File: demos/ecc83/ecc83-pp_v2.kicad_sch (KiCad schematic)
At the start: 15 parts, among them P1 IN, P2 OUT, P3 POWER, P4 CONN_2, P5 CONN_1, P6 CONN_1, P7 CONN_1, P8 CONN_1, U1 ECC83

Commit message: Demos update
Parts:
- U: renamed from R1; value 1.5K -> (none); footprint Resistor_THT:R_Axial_DIN0207_L6.3mm_D2.5mm_P7.62mm_Horizontal -> (none)
- U: renamed from R2; value 1.5K -> (none); footprint Resistor_THT:R_Axial_DIN0207_L6.3mm_D2.5mm_P7.62mm_Horizontal -> (none)
- U: renamed from R4; value 47K -> (none); footprint Resistor_THT:R_Axial_DIN0207_L6.3mm_D2.5mm_P7.62mm_Horizontal -> (none)
- U: renamed from R3; value 100K -> (none); footprint Resistor_THT:R_Axial_DIN0207_L6.3mm_D2.5mm_P7.62mm_Horizontal -> (none)
- U: renamed from C2; value 680nF -> (none); footprint Capacitors_THT:C_Axial_L12.0mm_D6.5mm_P20.00mm_Horizontal -> (none)
- U: renamed from P1; value IN -> (none); footprint Connector_PinHeader_2.54mm:PinHeader_1x02_P2.54mm_Vertical -> (none)
- U: renamed from P2; value OUT -> (none); footprint Connector_PinHeader_2.54mm:PinHeader_1x02_P2.54mm_Vertical -> (none)
- U: renamed from P3; value POWER -> (none); footprint Connector_PinHeader_2.54mm:PinHeader_1x02_P2.54mm_Vertical -> (none)
- U: renamed from C1; value 10uF -> (none); footprint Capacitor_THT:CP_Radial_D12.5mm_P7.50mm -> (none)
- U: renamed from P4; value CONN_2 -> (none); footprint Connector_PinHeader_2.54mm:PinHeader_1x02_P2.54mm_Vertical -> (none)
- U: renamed from U1; value ECC83 -> (none); footprint Valve:Valve_ECC-83-2 -> (none)
- U: renamed from P5; value CONN_1 -> (none); footprint connect:1pin -> (none)
- U: renamed from P6; value CONN_1 -> (none); footprint connect:1pin -> (none)
- U: renamed from P7; value CONN_1 -> (none); footprint connect:1pin -> (none)
- U: renamed from P8; value CONN_1 -> (none); footprint connect:1pin -> (none)
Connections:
- net at U.1, U.7 (G): now also U.6 (A); no longer U.1 (A)
- net at U.1: now also U.8 (K); no longer U.3 (K)
- net at U.1, U.2 (PM): now also U.7 (G); no longer U.2 (G)
- net at U.2 (PM): no longer U.9 (F2)
- now unconnected: U.1 (P1)

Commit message: Demos update.
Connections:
- net at U.1, U.7 (G): now also U.1 (A); no longer U.6 (A)
- net at U.1: now also U.3 (K); no longer U.8 (K)
- net at U.1, U.2 (PM): now also U.2 (G); no longer U.7 (G)
- net at U.1 (P1): now also U.4 (F1), U.5 (F1)
- net at U.2 (PM): now also U.9 (F2)
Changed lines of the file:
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@@
-(kicad_sch (version 20220404) (generator eeschema)
+(kicad_sch (version 20220822) (generator eeschema)
   (paper "A4")
   (title_block
@@
     (pin "7")
     (pin "8")
+  )
+  (symbol (lib_id "ecc83_schlib:ECC83") (at 165.1 106.68 0) (unit 2)
+    (in_bom yes) (on_board yes)
+    (default_instance (reference "U") (unit 1) (value "") (footprint ""))
+    (property "Reference" "U" (id 0) (at 177.8 104.14 0)
+      (effects (font (size 1.27 1.27)))
+    )
+    (property "Value" "" (id 1) (at 177.8 106.68 0)
+      (effects (font (size 1.27 1.27)))
+    )
+    (property "Footprint" "" (id 2) (at 177.8 109.22 0)
+      (effects (font (size 0.762 0.762)))
+    )
+    (property "Datasheet" "" (id 3) (at 165.1 106.68 0)
+      (effects (font (size 1.524 1.524)) hide)
+    )
     (pin "1")
     (pin "2")
     (pin "3")
+  )
+  (symbol (lib_id "ecc83_schlib:ECC83") (at 99.06 77.47 0) (unit 3)
+    (in_bom yes) (on_board yes)
+    (default_instance (reference "U") (unit 1) (value "") (footprint ""))
+    (property "Reference" "U" (id 0) (at 106.68 74.93 0)
+      (effects (font (size 1.27 1.27)))
+    )
+    (property "Value" "" (id 1) (at 107.95 77.47 0)
+      (effects (font (size 1.27 1.27)))
+    )
+    (property "Footprint" "" (id 2) (at 111.76 80.01 0)
+      (effects (font (size 0.762 0.762)))
+    )
+    (property "Datasheet" "" (id 3) (at 99.06 77.47 0)
+      (effects (font (size 1.524 1.524)) hide)
+    )
     (pin "4")
     (pin "5")
-    (pin "9")
-  )
-  (symbol (lib_id "ecc83_schlib:ECC83") (at 165.1 106.68 0) (unit 1)
-    (in_bom yes) (on_board yes)
-    (default_instance (reference "U") (unit 1) (value "") (footprint ""))
-    (property "Reference" "U" (id 0) (at 177.8 104.14 0)
-      (effects (font (size 1.27 1.27)))
-    )
-    (property "Value" "" (id 1) (at 177.8 106.68 0)
-      (effects (font (size 1.27 1.27)))
-    )
-    (property "Footprint" "" (id 2) (at 177.8 109.22 0)
-      (effects (font (size 0.762 0.762)))
-    )
-    (property "Datasheet" "" (id 3) (at 165.1 106.68 0)
-      (effects (font (size 1.524 1.524)) hide)
-    )
-    (pin "6")
-    (pin "7")
-    (pin "8")
-    (pin "1")
-    (pin "2")
-    (pin "3")
-    (pin "4")
-    (pin "5")
-    (pin "9")
-  )
-  (symbol (lib_id "ecc83_schlib:ECC83") (at 99.06 77.47 0) (unit 1)
-    (in_bom yes) (on_board yes)
-    (default_instance (reference "U") (unit 1) (value "") (footprint ""))
-    (property "Reference" "U" (id 0) (at 106.68 74.93 0)
-      (effects (font (size 1.27 1.27)))
-    )
-    (property "Value" "" (id 1) (at 107.95 77.47 0)
-      (effects (font (size 1.27 1.27)))
-    )
-    (property "Footprint" "" (id 2) (at 111.76 80.01 0)
-      (effects (font (size 0.762 0.762)))
-    )
-    (property "Datasheet" "" (id 3) (at 99.06 77.47 0)
-      (effects (font (size 1.524 1.524)) hide)
-    )
-    (pin "6")
-    (pin "7")
-    (pin "8")
-    (pin "1")
-    (pin "2")
-    (pin "3")
-    (pin "4")
-    (pin "5")

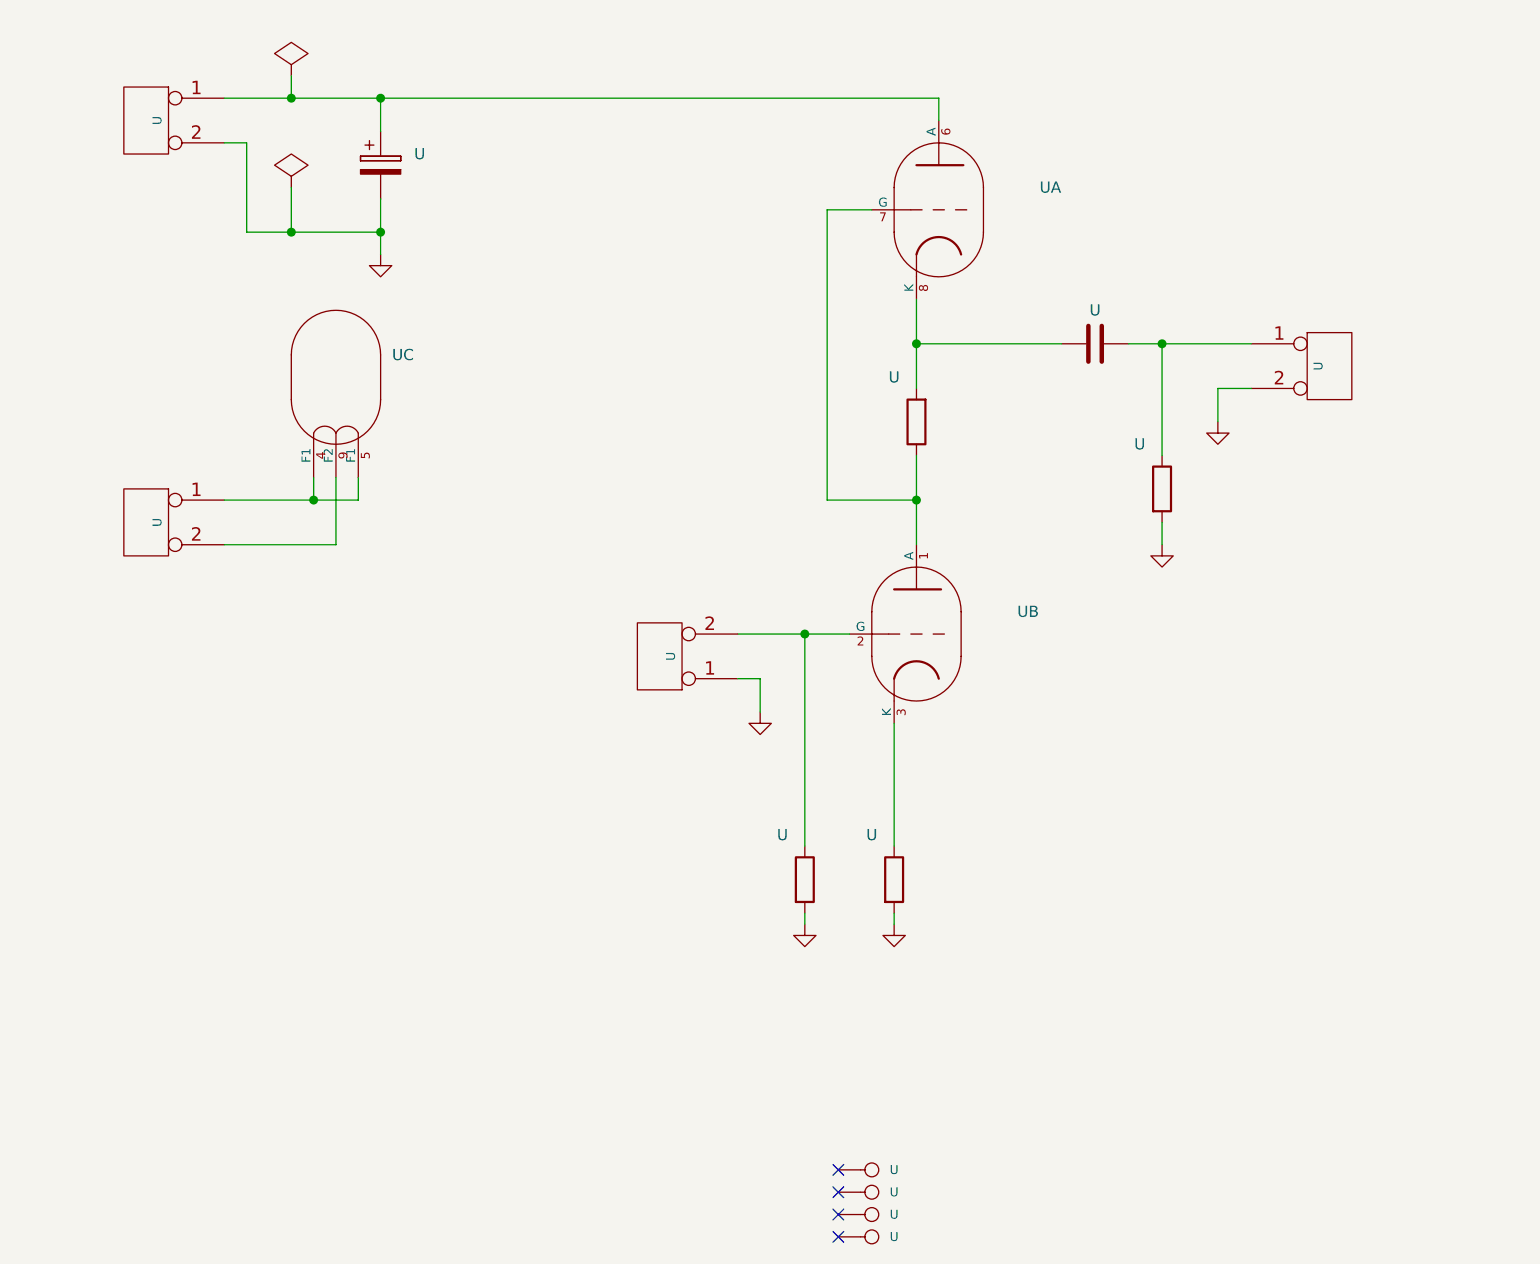
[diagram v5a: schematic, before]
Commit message: Update demos using latest file formats.
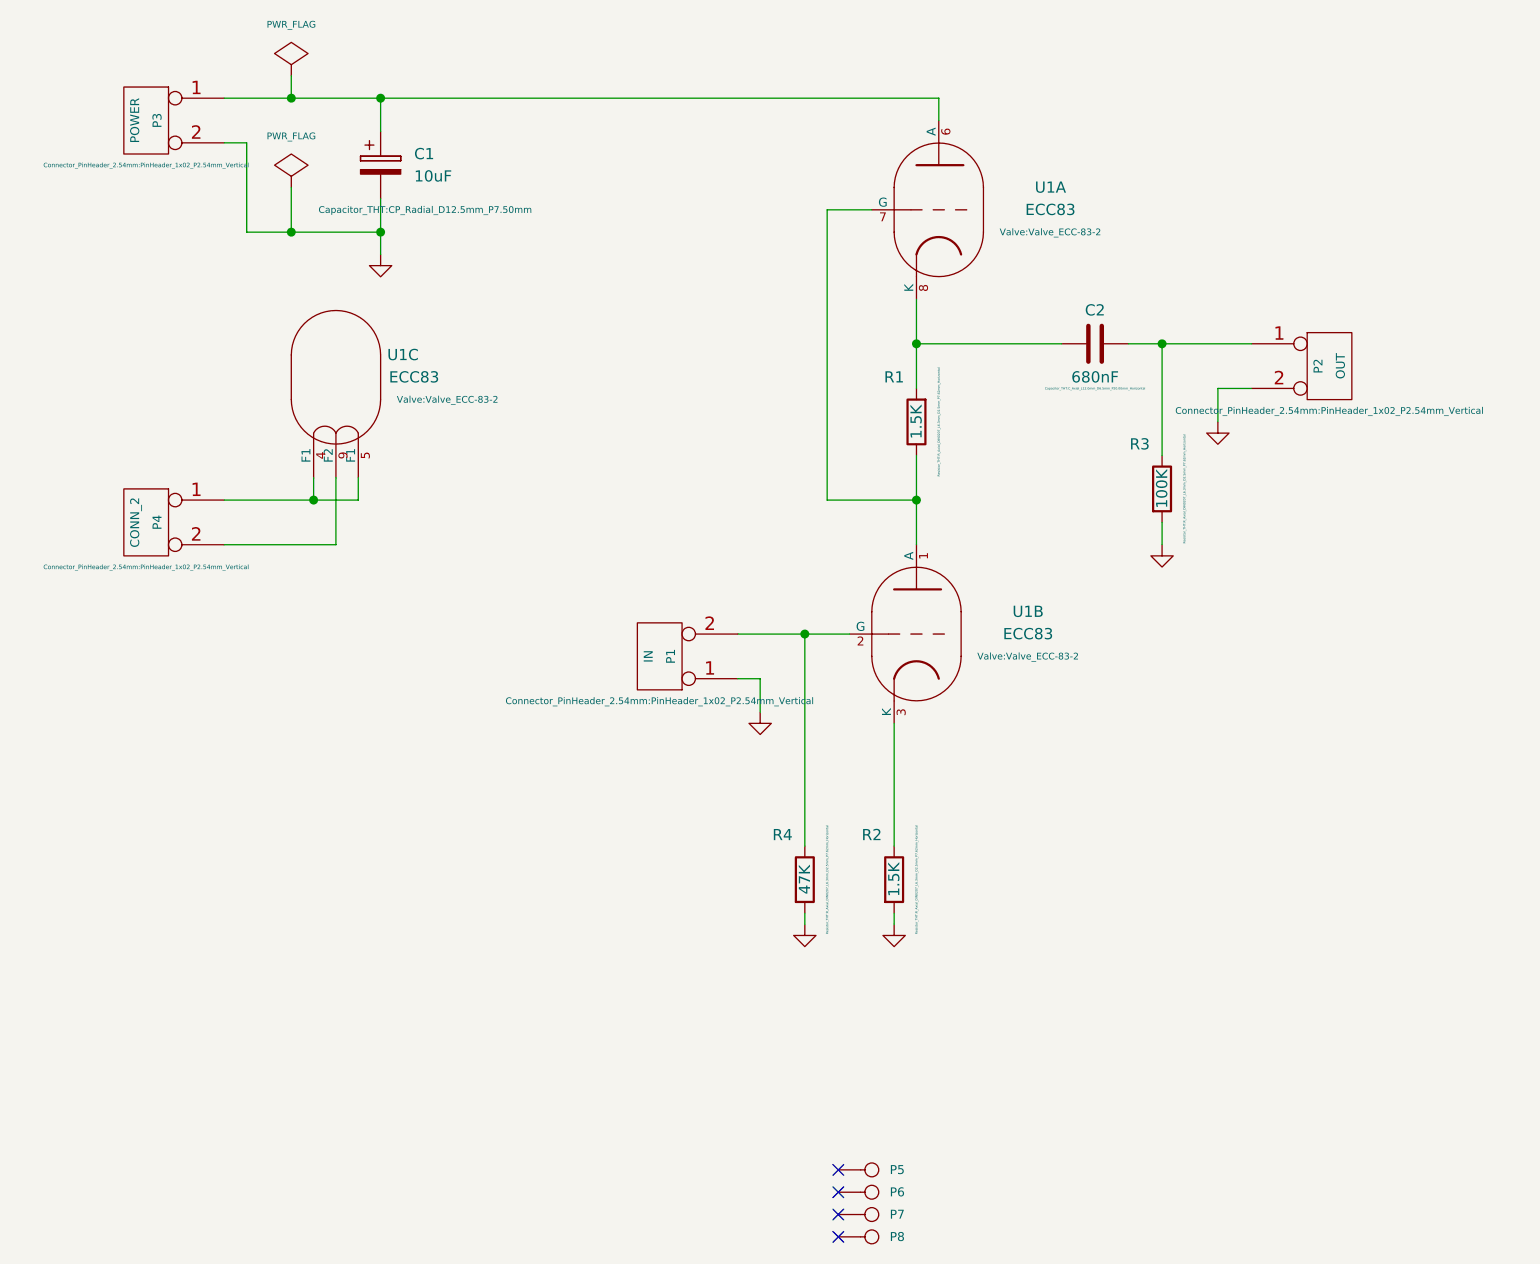
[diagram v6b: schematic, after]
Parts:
- C1: renamed from U; value (none) -> 10uF; footprint (none) -> Capacitor_THT:CP_Radial_D12.5mm_P7.50mm
- C2: renamed from U; value (none) -> 680nF; footprint (none) -> Capacitor_THT:C_Axial_L12.0mm_D6.5mm_P20.00mm_Horizontal
- P1: renamed from U; value (none) -> IN; footprint (none) -> Connector_PinHeader_2.54mm:PinHeader_1x02_P2.54mm_Vertical
- P2: renamed from U; value (none) -> OUT; footprint (none) -> Connector_PinHeader_2.54mm:PinHeader_1x02_P2.54mm_Vertical
- P3: renamed from U; value (none) -> POWER; footprint (none) -> Connector_PinHeader_2.54mm:PinHeader_1x02_P2.54mm_Vertical
- P4: renamed from U; value (none) -> CONN_2; footprint (none) -> Connector_PinHeader_2.54mm:PinHeader_1x02_P2.54mm_Vertical
- P5, P6, P7, P8: renamed from U; value (none) -> CONN_1; footprint (none) -> connect:1pin
- R1, R2: renamed from U; value (none) -> 1.5K; footprint (none) -> Resistor_THT:R_Axial_DIN0207_L6.3mm_D2.5mm_P7.62mm_Horizontal
- R3: renamed from U; value (none) -> 100K; footprint (none) -> Resistor_THT:R_Axial_DIN0207_L6.3mm_D2.5mm_P7.62mm_Horizontal
- R4: renamed from U; value (none) -> 47K; footprint (none) -> Resistor_THT:R_Axial_DIN0207_L6.3mm_D2.5mm_P7.62mm_Horizontal
- U1: renamed from U; value (none) -> ECC83; footprint (none) -> Valve:Valve_ECC-83-2
